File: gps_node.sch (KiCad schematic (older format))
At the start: 50 parts

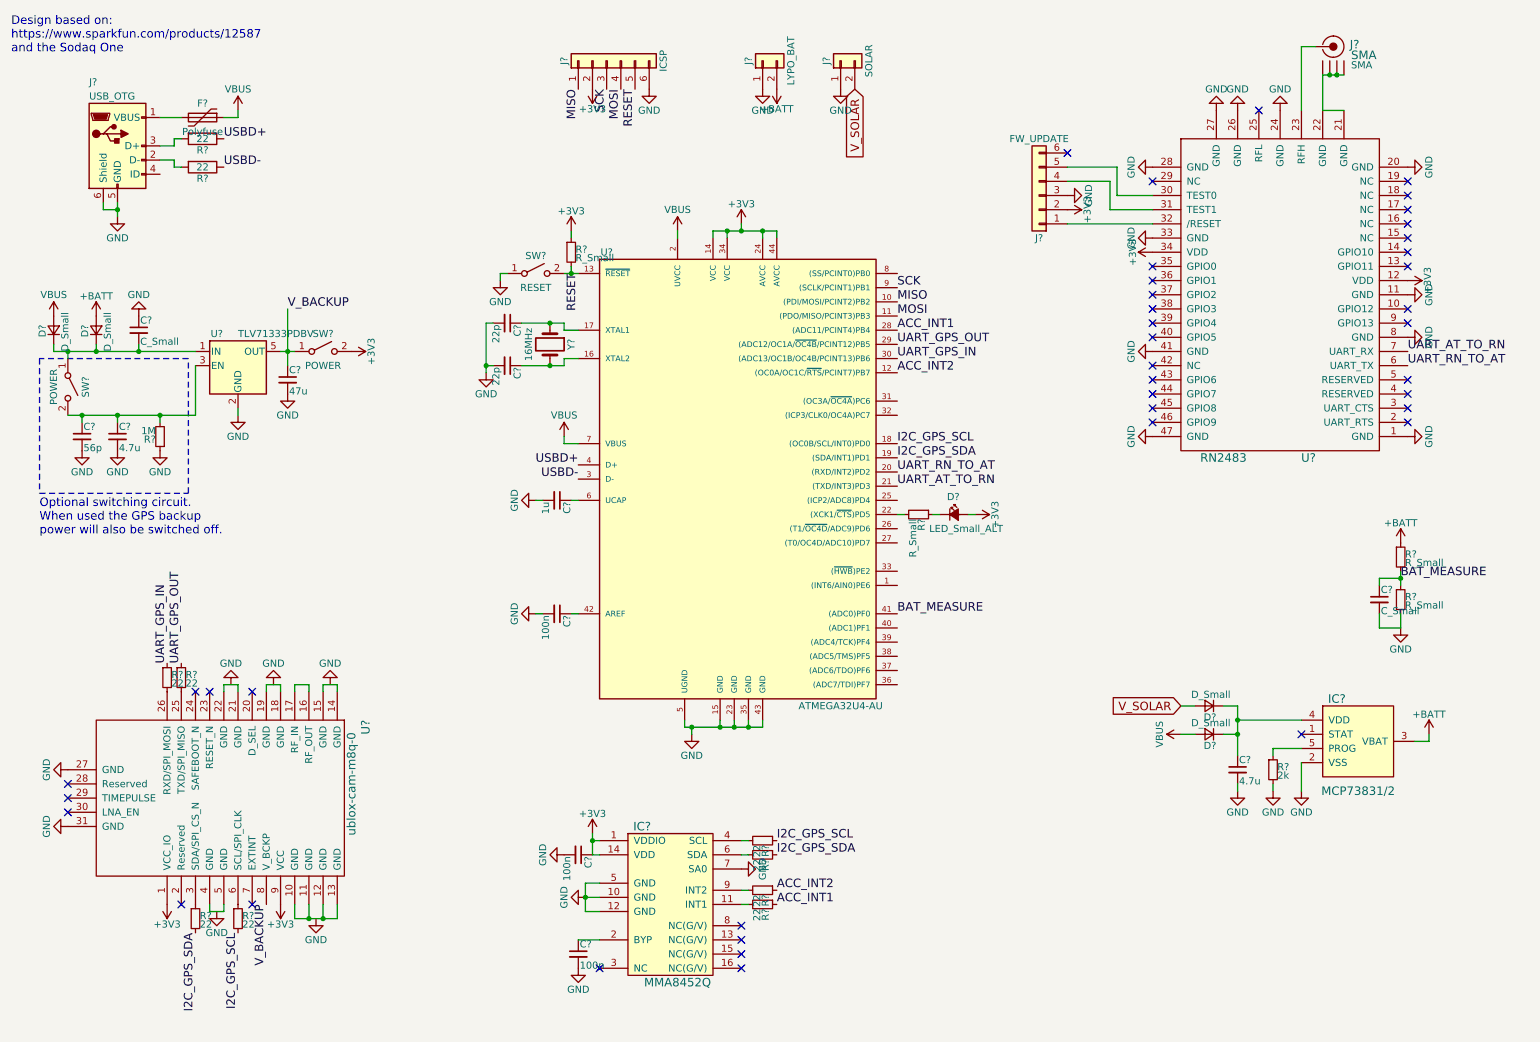
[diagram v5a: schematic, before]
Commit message: Cleaned up schematic, change avrisp component
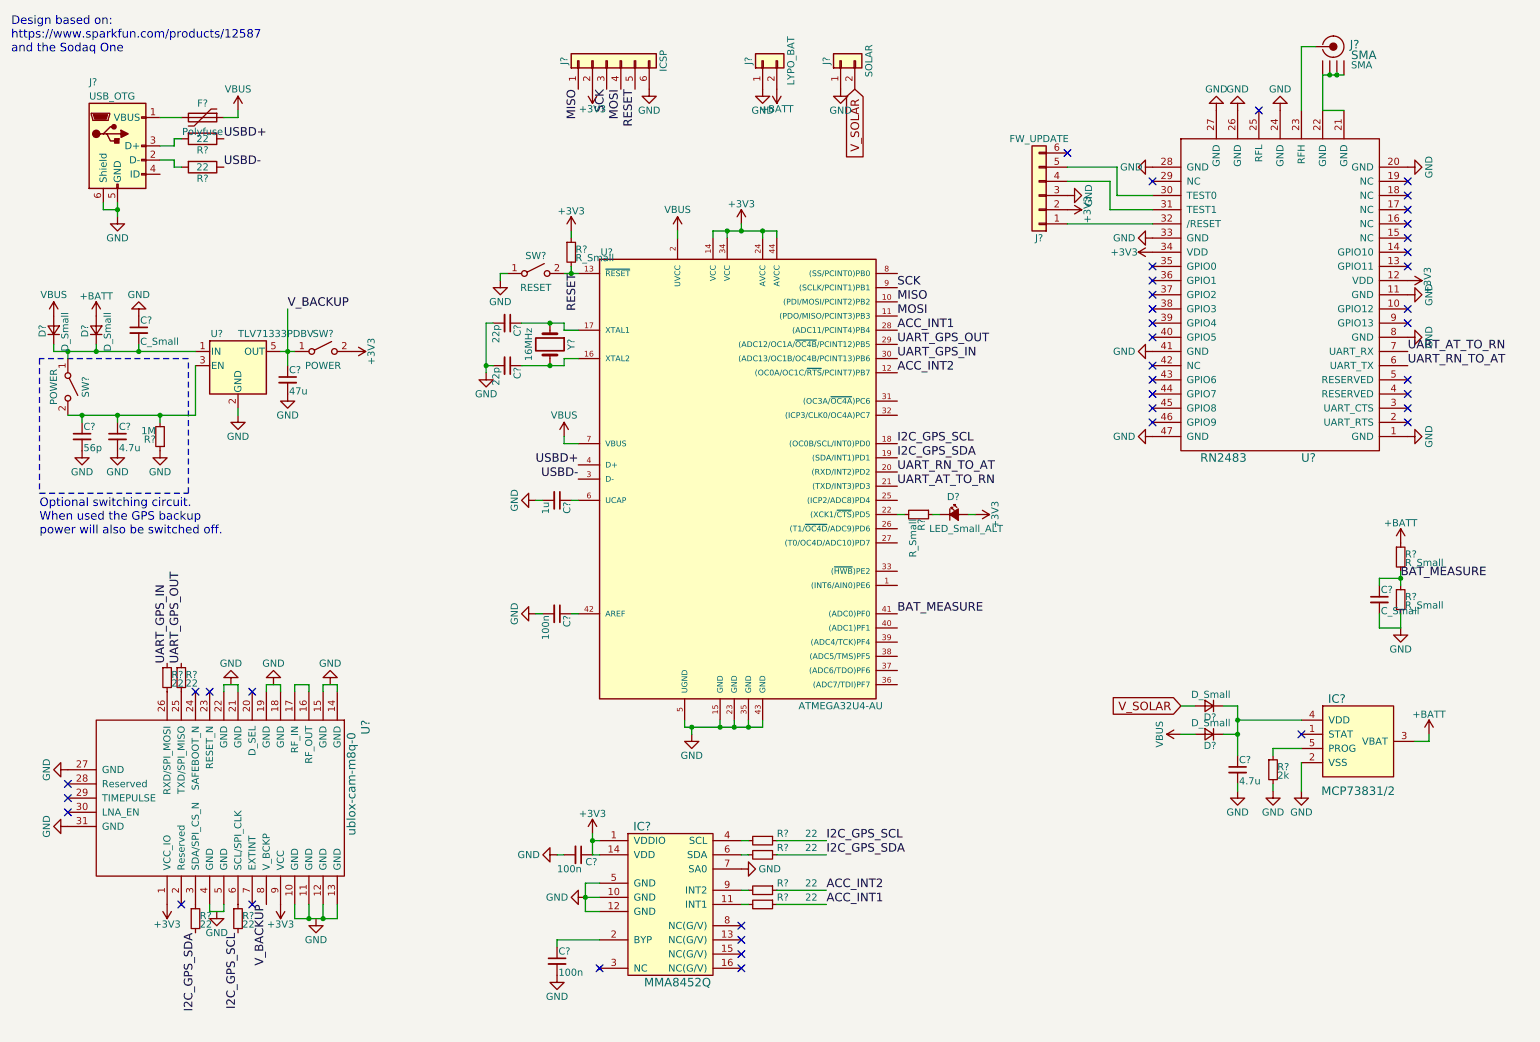
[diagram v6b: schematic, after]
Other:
- moved on the sheet: C?
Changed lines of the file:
@@
 LIBS:power
 LIBS:device
-LIBS:switches
-LIBS:relays
-LIBS:motors
-LIBS:transistors
-LIBS:conn
 LIBS:linear
 LIBS:regul
-LIBS:74xx
-LIBS:cmos4000
 LIBS:adc-dac
 LIBS:memory
@@
 LIBS:digital-audio
 LIBS:philips
-LIBS:display
 LIBS:cypress
 LIBS:siliconi
@@
 LIBS:atmel
 LIBS:contrib
-LIBS:valves
-LIBS:uln-ic
-LIBS:transistor
-LIBS:ti-ic
-LIBS:stmicro-mcu
-LIBS:standard
-LIBS:sparkfun
-LIBS:sharp-relay
-LIBS:rohm
-LIBS:regulator
-LIBS:on-semi-ic
-LIBS:nxp-ic
-LIBS:microchip-ic
-LIBS:micrel-ic
-LIBS:maxim-ic
-LIBS:led
-LIBS:ftdi-ic
-LIBS:freescale-ic
-LIBS:diode-inc-ic
-LIBS:connector
-LIBS:bluegiga
-LIBS:avr-mcu
-LIBS:analog-ic
-LIBS:7400-ic
-LIBS:4000-ic
 LIBS:drawn_by_jpmeijers
 LIBS:gps_node-cache
@@
 P 8600 1600
 F 0 "#PWR?" H 8600 1350 50  0001 C CNN
-F 1 "GND" H 8600 1450 50  0000 C CNN
+F 1 "GND" V 8600 1450 50  0000 C CNN
 F 2 "" H 8600 1600 50  0001 C CNN
 F 3 "" H 8600 1600 50  0001 C CNN
@@
 P 8600 2100
 F 0 "#PWR?" H 8600 1850 50  0001 C CNN
-F 1 "GND" H 8600 1950 50  0000 C CNN
+F 1 "GND" V 8600 1900 50  0000 C CNN
 F 2 "" H 8600 2100 50  0001 C CNN
 F 3 "" H 8600 2100 50  0001 C CNN
@@
 P 8600 2900
 F 0 "#PWR?" H 8600 2650 50  0001 C CNN
-F 1 "GND" H 8600 2750 50  0000 C CNN
+F 1 "GND" V 8600 2700 50  0000 C CNN
 F 2 "" H 8600 2900 50  0001 C CNN
 F 3 "" H 8600 2900 50  0001 C CNN
@@
 P 8600 3500
 F 0 "#PWR?" H 8600 3250 50  0001 C CNN
-F 1 "GND" H 8600 3350 50  0000 C CNN
+F 1 "GND" V 8600 3300 50  0000 C CNN
 F 2 "" H 8600 3500 50  0001 C CNN
 F 3 "" H 8600 3500 50  0001 C CNN
@@
 P 8600 2200
 F 0 "#PWR?" H 8600 2050 50  0001 C CNN
-F 1 "+3V3" H 8600 2340 50  0000 C CNN
+F 1 "+3V3" V 8600 2400 50  0000 C CNN
 F 2 "" H 8600 2200 50  0001 C CNN
 F 3 "" H 8600 2200 50  0001 C CNN
@@
 	1800 2950 750  2950
 Wire Wire Line
-	4700 6850 4600 6850
-Wire Wire Line
-	4600 6850 4600 6650
+	4600 6850 4700 6850
+Wire Wire Line
+	4600 6650 4600 6850
 Wire Wire Line
 	4600 6650 4700 6650
@@
 P 4600 6750
 F 0 "#PWR?" H 4600 6500 50  0001 C CNN
-F 1 "GND" H 4600 6600 50  0000 C CNN
+F 1 "GND" V 4600 6550 50  0000 C CNN
 F 2 "" H 4600 6750 50  0001 C CNN
 F 3 "" H 4600 6750 50  0001 C CNN
@@
 NoConn ~ 5700 6950
 NoConn ~ 4700 7250
-Text Label 5950 6450 0    60   ~ 0
+Text Label 6300 6450 0    60   ~ 0
 I2C_GPS_SDA
-Text Label 5950 6350 0    60   ~ 0
+Text Label 6300 6350 0    60   ~ 0
 I2C_GPS_SCL
 $Comp
@@
 U 1 1 5A2DD111
 P 5850 6350
-F 0 "R?" H 5880 6370 50  0000 L CNN
-F 1 "22" H 5880 6310 50  0000 L CNN
+F 0 "R?" V 5800 6450 50  0000 L CNN
+F 1 "22" V 5800 6650 50  0000 L CNN
 F 2 "" H 5850 6350 50  0001 C CNN
 F 3 "" H 5850 6350 50  0001 C CNN
@@
 U 1 1 5A2DD2C3
 P 5850 6450
-F 0 "R?" H 5880 6470 50  0000 L CNN
-F 1 "22" H 5880 6410 50  0000 L CNN
+F 0 "R?" V 5800 6550 50  0000 L CNN
+F 1 "22" V 5800 6750 50  0000 L CNN
 F 2 "" H 5850 6450 50  0001 C CNN
 F 3 "" H 5850 6450 50  0001 C CNN
@@
 U 1 1 5A2DD354
 P 5850 6800
-F 0 "R?" H 5880 6820 50  0000 L CNN
-F 1 "22" H 5880 6760 50  0000 L CNN
+F 0 "R?" V 5800 6900 50  0000 L CNN
+F 1 "22" V 5800 7100 50  0000 L CNN
 F 2 "" H 5850 6800 50  0001 C CNN
 F 3 "" H 5850 6800 50  0001 C CNN
@@
 U 1 1 5A2DD3F8
 P 5850 6700
-F 0 "R?" H 5880 6720 50  0000 L CNN
-F 1 "22" H 5880 6660 50  0000 L CNN
+F 0 "R?" V 5800 6800 50  0000 L CNN
+F 1 "22" V 5800 7000 50  0000 L CNN
 F 2 "" H 5850 6700 50  0001 C CNN
 F 3 "" H 5850 6700 50  0001 C CNN
@@
 L C_Small C?
 U 1 1 5A2DE4C9
-P 4550 7150
-F 0 "C?" H 4560 7220 50  0000 L CNN
-F 1 "100n" H 4560 7070 50  0000 L CNN
-F 2 "" H 4550 7150 50  0001 C CNN
-F 3 "" H 4550 7150 50  0001 C CNN
-	1    4550 7150
-	1    0    0    -1
-$EndComp
-Wire Wire Line
-	4550 7050 4700 7050
+P 4400 7200
+F 0 "C?" H 4410 7270 50  0000 L CNN
+F 1 "100n" H 4410 7120 50  0000 L CNN
+F 2 "" H 4400 7200 50  0001 C CNN
+F 3 "" H 4400 7200 50  0001 C CNN
+	1    4400 7200
+	1    0    0    -1
+$EndComp
+Wire Wire Line
+	4400 7050 4700 7050
 $Comp
 L GND #PWR?
 U 1 1 5A2DE686
-P 4550 7250
-F 0 "#PWR?" H 4550 7000 50  0001 C CNN
-F 1 "GND" H 4550 7100 50  0000 C CNN
-F 2 "" H 4550 7250 50  0001 C CNN
-F 3 "" H 4550 7250 50  0001 C CNN
-	1    4550 7250
+P 4400 7300
+F 0 "#PWR?" H 4400 7050 50  0001 C CNN
+F 1 "GND" H 4400 7150 50  0000 C CNN
+F 2 "" H 4400 7300 50  0001 C CNN
+F 3 "" H 4400 7300 50  0001 C CNN
+	1    4400 7300
 	1    0    0    -1
 $EndComp
@@
 U 1 1 5A2DE7B7
 P 4550 6450
-F 0 "C?" H 4560 6520 50  0000 L CNN
-F 1 "100n" H 4560 6370 50  0000 L CNN
+F 0 "C?" V 4600 6500 50  0000 L CNN
+F 1 "100n" V 4650 6300 50  0000 L CNN
 F 2 "" H 4550 6450 50  0001 C CNN
 F 3 "" H 4550 6450 50  0001 C CNN
@@
 L GND #PWR?
 U 1 1 5A2DE87B
-P 4450 6450
-F 0 "#PWR?" H 4450 6200 50  0001 C CNN
-F 1 "GND" H 4450 6300 50  0000 C CNN
-F 2 "" H 4450 6450 50  0001 C CNN
-F 3 "" H 4450 6450 50  0001 C CNN
-	1    4450 6450
+P 4400 6450
+F 0 "#PWR?" H 4400 6200 50  0001 C CNN
+F 1 "GND" V 4400 6250 50  0000 C CNN
+F 2 "" H 4400 6450 50  0001 C CNN
+F 3 "" H 4400 6450 50  0001 C CNN
+	1    4400 6450
 	0    1    1    0
 $EndComp
@@
 P 5700 6550
 F 0 "#PWR?" H 5700 6300 50  0001 C CNN
-F 1 "GND" H 5700 6400 50  0000 C CNN
+F 1 "GND" V 5700 6350 50  0000 C CNN
 F 2 "" H 5700 6550 50  0001 C CNN
 F 3 "" H 5700 6550 50  0001 C CNN
@@
 Wire Wire Line
 	5700 6800 5750 6800
-Text Label 5950 6800 0    60   ~ 0
+Text Label 6300 6800 0    60   ~ 0
 ACC_INT1
-Text Label 5950 6700 0    60   ~ 0
+Text Label 6300 6700 0    60   ~ 0
 ACC_INT2
 Text Label 6800 2750 0    60   ~ 0
@@
 Text Label 6800 2550 0    60   ~ 0
 MISO
+Wire Wire Line
+	5950 6800 6300 6800
+Wire Wire Line
+	5950 6700 6300 6700
+Wire Wire Line
+	5950 6350 6300 6350
+Wire Wire Line
+	6300 6450 5950 6450
+Wire Wire Line
+	4400 7050 4400 7100
+Wire Wire Line
+	4450 6450 4400 6450
 $EndSCHEMATC

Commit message: Add status LEDs for charger
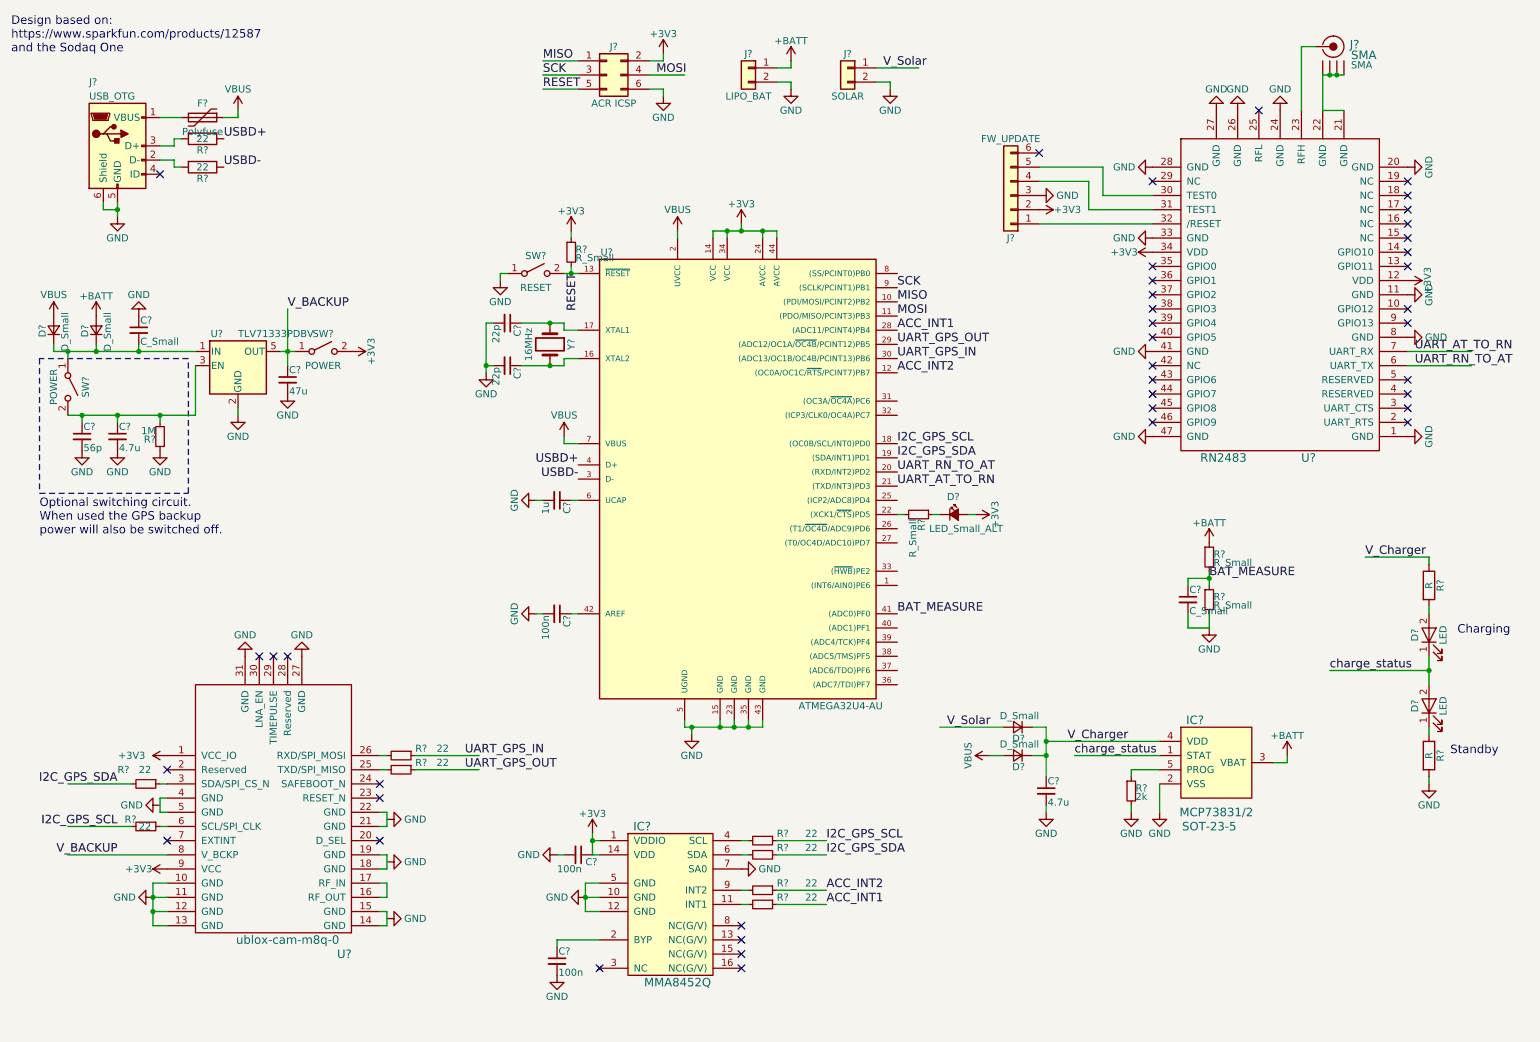
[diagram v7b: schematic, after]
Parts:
- removed J?: ICSP, symbol Conn_01x06
- added D? (x2): LED, symbol LED
- added J?: ACR ICSP, symbol Conn_02x03_Odd_Even
- added R? (x2): R, symbol R
- IC?: footprint (none) -> SOT-23-5
- J?: value LYPO_BAT -> LIPO_BAT
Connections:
- net labels added: V_Charger, V_Solar, charge_status
- net labels removed: V_SOLAR
- wire segments 131 -> 165
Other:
- note added: "Charging"
- note added: "Standby"
- moved on the sheet: C?, D?, IC?, J?, R?, U?
